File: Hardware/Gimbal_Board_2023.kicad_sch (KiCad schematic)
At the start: 76 parts, among them J1 6P6C, J2 RJ45_LED_Shielded, Q1 Q_NMOS_GDS, Q2 Q_NMOS_GDS, Q3 Q_NMOS_GDS, Q4 Q_NMOS_GDS, Q5 Q_NMOS_GDS, Q6 Q_NMOS_GDS, Q7 Q_NMOS_GDS, Q8 Q_NMOS_GDS, SW1 SW_Push, SW2 SW_Push, SW3 SW_Push, SW4 SW_Push, SW5 SW_Push, SW6 SW_Push, SW7 SW_Push, SW8 SW_Push, SW9 SW_DPDT_x2, U1 OKI, U2 OKI, U3 Teensy4.1_DEV-16771

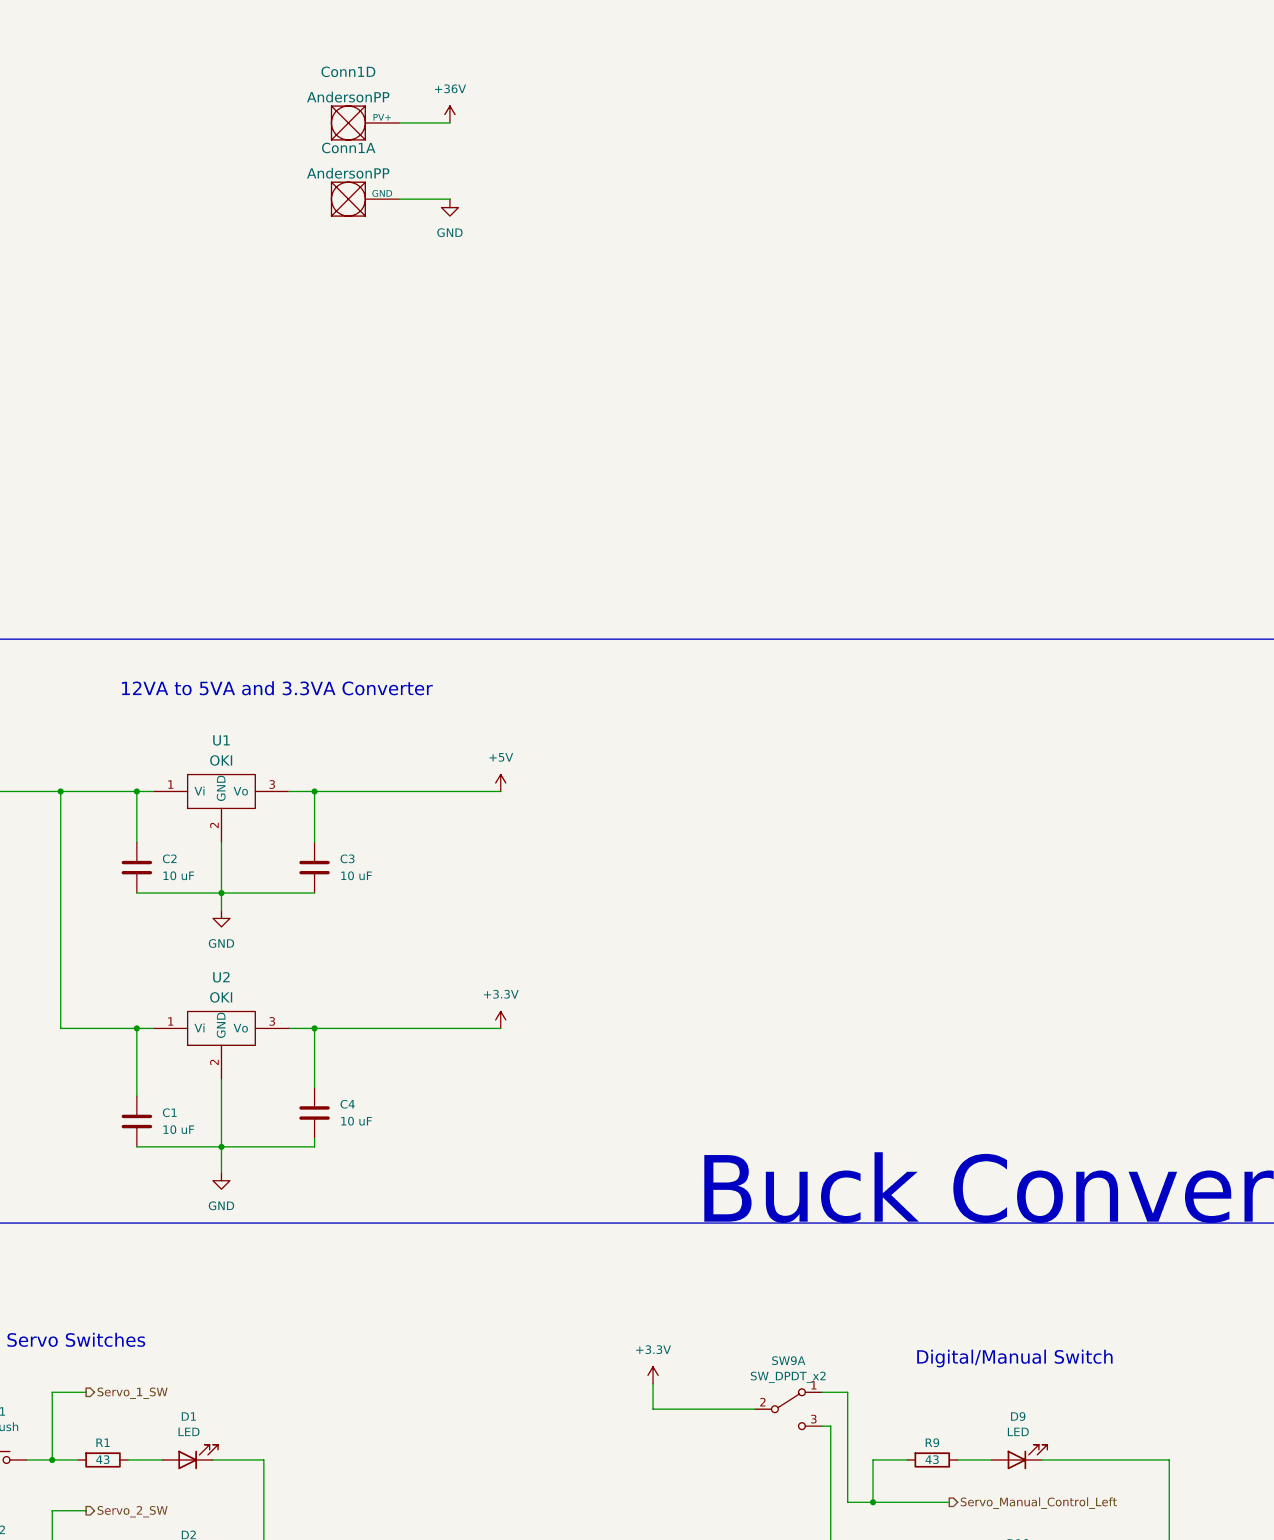
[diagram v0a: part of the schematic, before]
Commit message: schematic review changes
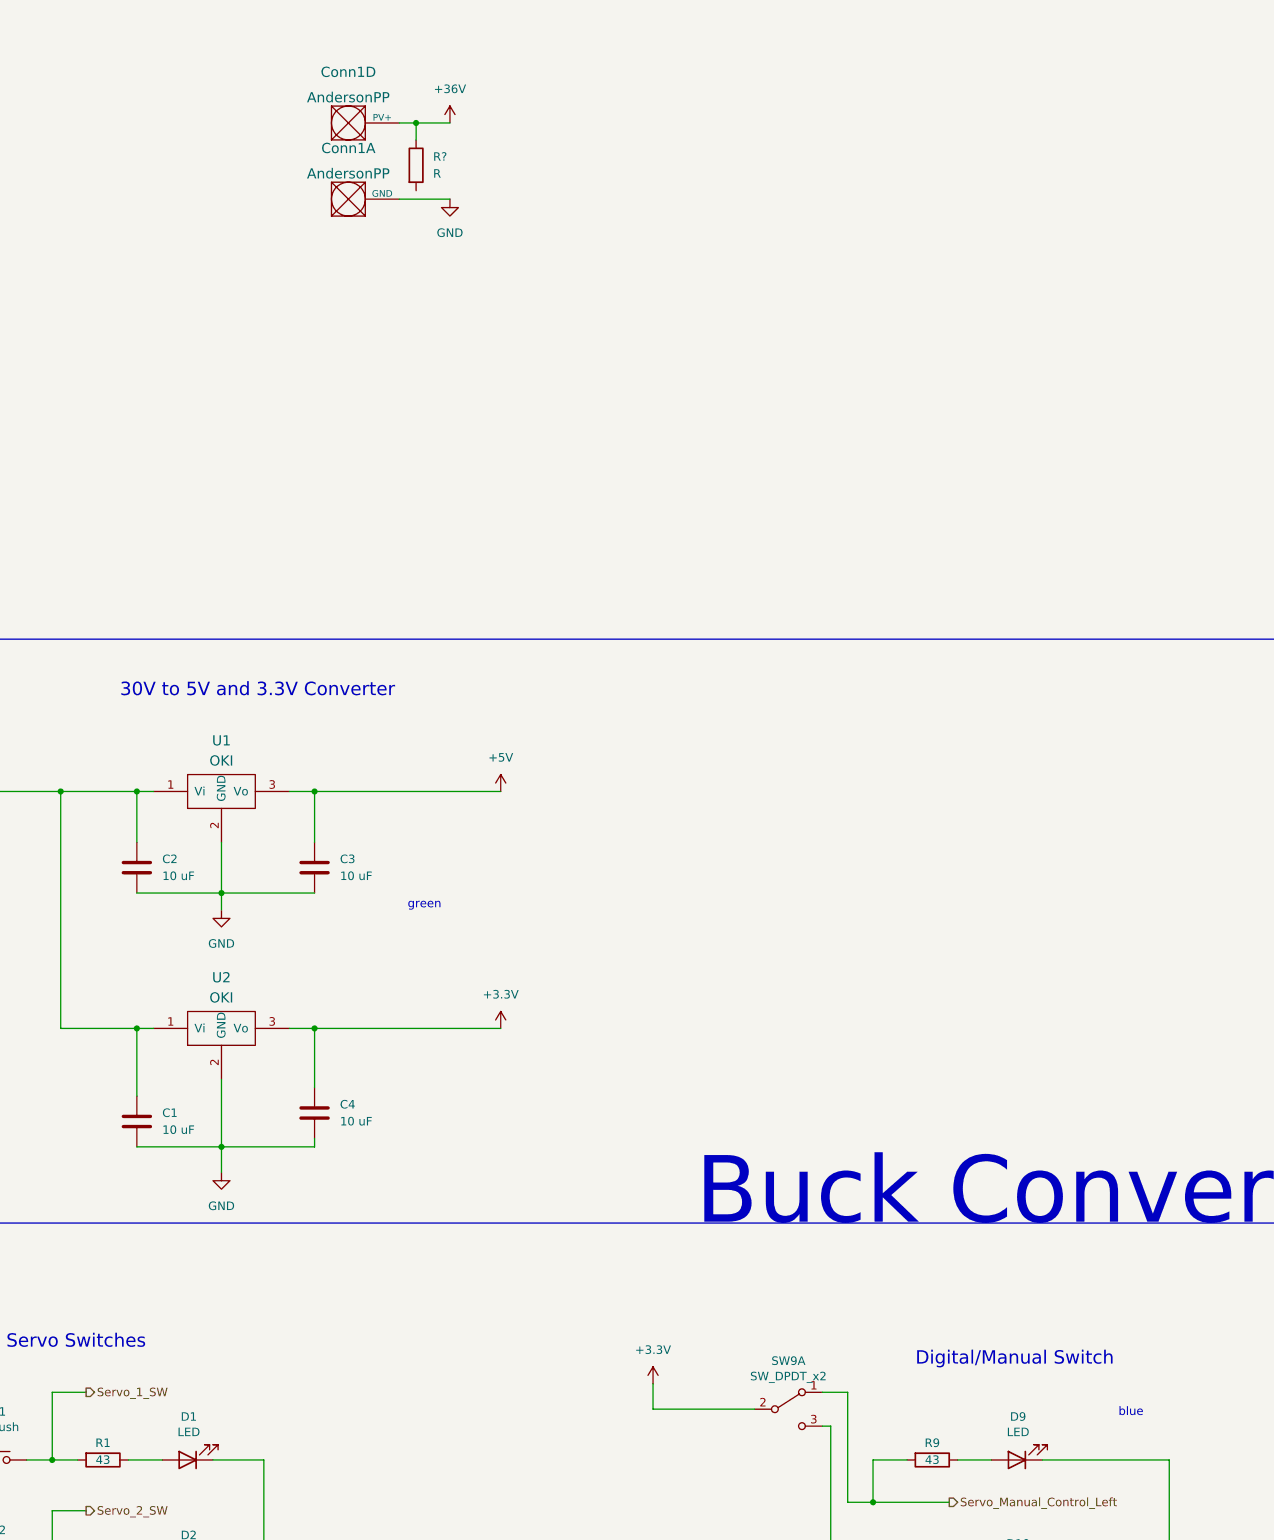
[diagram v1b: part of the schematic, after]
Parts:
- added R?: R, symbol Device:R
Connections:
- net +36V: now also R?.1
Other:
- note added: "30V to 5V and 3.3V Converter"
- note added: "blue"
- note added: "green"
- note removed: "12VA to 5VA and 3.3VA Converter"
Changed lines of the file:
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@@
 (kicad_sch (version 20211123) (generator eeschema)
-  (paper "A1")
+  (paper "A2")
   (junction (at 320.04 236.22) (diameter 0) (color 0 0 0 0)
   )
@@
   )
   (junction (at 320.04 312.42) (diameter 0) (color 0 0 0 0)
+  )
+  (junction (at 114.3 69.85) (diameter 0) (color 0 0 0 0)
   )
   (junction (at 38.1 270.51) (diameter 0) (color 0 0 0 0)
@@
     (stroke (width 0) (type default) (color 0 0 0 0))
   )
+  (wire (pts (xy 114.3 69.85) (xy 114.3 72.39))
+    (stroke (width 0) (type default) (color 0 0 0 0))
+  )
   (wire (pts (xy 422.91 53.34) (xy 422.91 54.61))
     (stroke (width 0) (type default) (color 0 0 0 0))
@@
     (stroke (width 0) (type default) (color 0 0 0 0))
   )
+  (wire (pts (xy 114.3 69.85) (xy 111.76 69.85))
+    (stroke (width 0) (type default) (color 0 0 0 0))
+  )
   (wire (pts (xy 361.95 198.12) (xy 368.3 198.12))
     (stroke (width 0) (type default) (color 0 0 0 0))
@@
     (stroke (width 0) (type default) (color 0 0 0 0))
   )
-  (wire (pts (xy 119.38 69.85) (xy 111.76 69.85))
+  (wire (pts (xy 119.38 69.85) (xy 114.3 69.85))
     (stroke (width 0) (type default) (color 0 0 0 0))
   )
@@
     (effects (font (size 10 10)) (justify left bottom))
   )
-  (text "12VA to 5VA and 3.3VA Converter" (at 69.85 156.21 0)
+  (text "30V to 5V and 3.3V Converter" (at 69.85 156.21 0)
     (effects (font (size 2.0066 2.0066)) (justify left bottom))
   )
@@
     (effects (font (size 10 10)) (justify left bottom))
   )
+  (text "blue" (at 219.71 264.16 0)
+    (effects (font (size 1.27 1.27)) (justify left bottom))
+  )
   (text "Digital/Manual Switch" (at 189.23 256.54 0)
     (effects (font (size 2.0066 2.0066)) (justify left bottom))
+  )
+  (text "green" (at 113.03 187.96 0)
+    (effects (font (size 1.27 1.27)) (justify left bottom))
   )
   (text "Servo Connectors" (at 326.39 342.9 0)
@@
     )
     (property "Datasheet" "~" (id 3) (at 50.8 283.21 0)
+      (effects (font (size 1.27 1.27)) hide)
+    )
+    (pin "1")
+    (pin "2")
+  )
+  (symbol (lib_id "Device:R") (at 114.3 76.2 0) (unit 1)
+    (in_bom yes) (on_board yes) (fields_autoplaced)
+    (property "Reference" "R?" (id 0) (at 116.84 74.9299 0)
+      (effects (font (size 1.27 1.27)) (justify left))
+    )
+    (property "Value" "R" (id 1) (at 116.84 77.4699 0)
+      (effects (font (size 1.27 1.27)) (justify left))
+    )
+    (property "Footprint" "" (id 2) (at 112.522 76.2 90)
+      (effects (font (size 1.27 1.27)) hide)
+    )
+    (property "Datasheet" "~" (id 3) (at 114.3 76.2 0)
       (effects (font (size 1.27 1.27)) hide)
     )
@@
       (reference "R26") (unit 1) (value "100") (footprint "Resistor_SMD:R_0603_1608Metric_Pad0.98x0.95mm_HandSolder")
     )
+    (path "/a0c7bf9a-d23c-4fed-bd06-b3d3eabfe30a"
+      (reference "R?") (unit 1) (value "R") (footprint "")
+    )
     (path "/6adce192-3da5-498a-88fe-8795f4fcfe04"

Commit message: Changed Manual Switches resistor value to 100 and added global label
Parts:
- added U? (x2): TSR_1-2450, Converter_DCDC:Converter_DCDC_TRACO_TSR-1_THT, symbol Regulator_Switching:TSR_1-2450
- R1, R10, R2, R3, R4, R5, R6, R7, R8, R9: value 43 -> 100
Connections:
- net Servo_3­_SW is gone; now on net Servo_3_SW: R3.2, SW3.2
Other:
- moved on the sheet: C1, C2, C3, C4, Conn1A, Conn1D, D1, D10, D2, D3, D4, D5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

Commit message: Named Leds and oke to tsr added more leds and 5 v resistor to 300
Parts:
- removed C1, C2, C3, C4: 10 uF, Capacitor_SMD:C_0603_1608Metric_Pad1.08x0.95mm_HandSolder, symbol Device:C
- removed R?: R, symbol Device:R
- removed U1, U2: OKI, MRDT_Devices:OKI_Horizontal, symbol MRDT_Devices:OKI
- added D? (x2): LED, symbol Device:LED
- added D?: LED, LED_SMD:LED_0603_1608Metric_Pad1.05x0.95mm_HandSolder, symbol Device:LED
- added J?: Conn_01x09, symbol Connector_Generic:Conn_01x09
- added R01: 3000, Resistor_SMD:R_0603_1608Metric_Pad0.98x0.95mm_HandSolder, symbol Device:R
- added R?: 100, Resistor_SMD:R_0603_1608Metric_Pad0.98x0.95mm_HandSolder, symbol Device:R
- added R?: 300, Resistor_SMD:R_0603_1608Metric_Pad0.98x0.95mm_HandSolder, symbol Device:R
- R19, R20, R21, R22, R23, R24, R25, R26: value 100 -> 300
- gave numbers to parts that had none: 2
- renumbered D17 to DBlue1, D18 to DBlue1
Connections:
- net +3.3V: now also U3.3.3 (Vout), R?.2
- net +36V: now also U3.3.1 (Vin), U5.1 (Vin), R01.2
- net +5V: now also U5.3 (Vout), R?.2
- net GND: now also U3.3.2 (GND), U5.2 (GND), D?.1 (K), D?.1 (K), D?.1 (K)
- new net: D?.2 (A), R?.1 (x2)
- new net: D?.2 (A), R01.1
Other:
- note added: "Blue"
- note added: "Green"
- moved on the sheet: Conn1A, U3.3, U5

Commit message: Added in 9 and 3 pin, redid some reference label
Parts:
- removed Conn2, Conn3, Conn4, Conn5: Molex_uF_D_06, MRDT_Connectors:MOLEX_uF_D_06_Horizontal, symbol MRDT_Connectors:Molex_uF_D_06
- removed J?: Conn_01x09, symbol Connector_Generic:Conn_01x09
- added Conn6, Conn7: Molex_SL_09, symbol MRDT_Connectors:Molex_SL_09
- added Conn8: Molex_SL_03, symbol MRDT_Connectors:Molex_SL_03
- gave numbers to parts that had none: 5
- renumbered DBlue1 to D17, DBlue1 to D18, R01 to R29
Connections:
- net +5V: now also Conn6.1, Conn6.4, Conn6.7, Conn7.1, Conn7.4, Conn7.7, Conn8.1
- net GND: now also Conn6.2, Conn6.5, Conn6.8, Conn7.2, Conn7.5, Conn7.8, Conn8.2
- net Servo_1_PWM: now also Conn6.3
- net Servo_2_PWM: now also Conn6.6
- net Servo_3_PWM: now also Conn6.9
- net Servo_4_PWM: now also Conn7.3
- net Servo_5_PWM: now also Conn7.6
- net Servo_6_PWM: now also Conn7.9
- net Servo_7_PWM: now also Conn8.3
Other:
- note added: "?"
- note removed: "blue"
